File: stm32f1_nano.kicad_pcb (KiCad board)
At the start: 2 copper layers, 43.2 x 17.8 mm, 45 parts, among them J1 Analog, J2 Digital, J3 TYPE-C-31-M-12, J5 DEBUG, U1 STM32F103C8T6, U2 W25Q128JVSIQ, U4 XC6206P332MR, U5 AMS1117-5.0, Y1 X322516MLB4SI

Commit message: #2 green and red LED are too bright
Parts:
- R1, R2, R3: value 300 -> 330
- R11: value 75 -> 200
- R4: value 75 -> 150
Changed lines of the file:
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@@
     (descr "Resistor SMD 0402 (1005 Metric), square (rectangular) end terminal, IPC_7351 nominal, (Body size source: IPC-SM-782 page 72, https://www.pcb-3d.com/wordpress/wp-content/uploads/ipc-sm-782a_amendment_1_and_2.pdf), generated with kicad-footprint-generator")
     (tags "resistor")
-    (property "Description" "62.5mW Thick Film Resistors ±100ppm/℃ ±1% 300Ω 0402  Chip Resistor - Surface Mount ROHS")
-    (property "JLCPCB Part #" "C25102")
+    (property "Description" "62.5mW Thick Film Resistors ±100ppm/℃ ±1% 330Ω 0402  Chip Resistor - Surface Mount ROHS")
+    (property "JLCPCB Part #" "C25104")
     (property "Manufacturer" "UNI-ROYAL(Uniroyal Elec)")
-    (property "Manufacturer_Name" "UNI-ROYAL(Uniroyal Elec)")
-    (property "Manufacturer_Part_Number" "0402WGF3000TCE")
-    (property "Partnumber" "0402WGF3000TCE")
+    (property "Partnumber" "0402WGF3300TCE")
     (property "Sheetfile" "stm32f1_nano.kicad_sch")
     (property "Sheetname" "")
@@
         (effects (font (size 1 1) (thickness 0.15)))
     )
-    (fp_text value "300" (at 0 1.17) (layer "F.Fab")
+    (fp_text value "330" (at 0 1.17) (layer "F.Fab")
         (effects (font (size 1 1) (thickness 0.15)))
     )
@@
     (descr "Resistor SMD 0402 (1005 Metric), square (rectangular) end terminal, IPC_7351 nominal, (Body size source: IPC-SM-782 page 72, https://www.pcb-3d.com/wordpress/wp-content/uploads/ipc-sm-782a_amendment_1_and_2.pdf), generated with kicad-footprint-generator")
     (tags "resistor")
-    (property "Description" "62.5mW Thick Film Resistors ±100ppm/℃ ±1% 300Ω 0402  Chip Resistor - Surface Mount ROHS")
-    (property "JLCPCB Part #" "C25102")
+    (property "Description" "62.5mW Thick Film Resistors ±100ppm/℃ ±1% 330Ω 0402  Chip Resistor - Surface Mount ROHS")
+    (property "JLCPCB Part #" "C25104")
     (property "Manufacturer" "UNI-ROYAL(Uniroyal Elec)")
-    (property "Manufacturer_Name" "UNI-ROYAL(Uniroyal Elec)")
-    (property "Manufacturer_Part_Number" "0402WGF3000TCE")
-    (property "Partnumber" "0402WGF3000TCE")
+    (property "Partnumber" "0402WGF3300TCE")
     (property "Sheetfile" "stm32f1_nano.kicad_sch")
     (property "Sheetname" "")
@@
         (effects (font (size 1 1) (thickness 0.15)))
     )
-    (fp_text value "300" (at 0 1.17) (layer "F.Fab")
+    (fp_text value "330" (at 0 1.17) (layer "F.Fab")
         (effects (font (size 1 1) (thickness 0.15)))
     )
@@
     (descr "Resistor SMD 0402 (1005 Metric), square (rectangular) end terminal, IPC_7351 nominal, (Body size source: IPC-SM-782 page 72, https://www.pcb-3d.com/wordpress/wp-content/uploads/ipc-sm-782a_amendment_1_and_2.pdf), generated with kicad-footprint-generator")
     (tags "resistor")
-    (property "Description" "62.5mW Thick Film Resistors ±100ppm/℃ ±1% 75Ω 0402  Chip Resistor - Surface Mount ROHS")
-    (property "JLCPCB Part #" "C25133")
+    (property "Description" "62.5mW Thick Film Resistors ±100ppm/℃ ±1% 150Ω 0402  Chip Resistor - Surface Mount ROHS")
+    (property "JLCPCB Part #" "C25082")
     (property "Manufacturer" "UNI-ROYAL(Uniroyal Elec)")
-    (property "Manufacturer_Name" "UNI-ROYAL(Uniroyal Elec)")
-    (property "Manufacturer_Part_Number" "0402WGF750JTCE")
-    (property "Partnumber" "0402WGF750JTCE")
+    (property "Partnumber" "0402WGF1500TCE")
     (property "Sheetfile" "stm32f1_nano.kicad_sch")
     (property "Sheetname" "")
@@
         (effects (font (size 1 1) (thickness 0.15)))
     )
-    (fp_text value "75" (at 0 1.17) (layer "F.Fab")
+    (fp_text value "150" (at 0 1.17) (layer "F.Fab")
         (effects (font (size 1 1) (thickness 0.15)))
     )
@@
     (descr "Resistor SMD 0402 (1005 Metric), square (rectangular) end terminal, IPC_7351 nominal, (Body size source: IPC-SM-782 page 72, https://www.pcb-3d.com/wordpress/wp-content/uploads/ipc-sm-782a_amendment_1_and_2.pdf), generated with kicad-footprint-generator")
     (tags "resistor")
-    (property "Description" "62.5mW Thick Film Resistors ±100ppm/℃ ±1% 75Ω 0402  Chip Resistor - Surface Mount ROHS")
-    (property "JLCPCB Part #" "C25133")
+    (property "Description" "62.5mW Thick Film Resistors ±100ppm/℃ ±1% 200Ω 0402  Chip Resistor - Surface Mount ROHS")
+    (property "JLCPCB Part #" "C25087")
     (property "Manufacturer" "UNI-ROYAL(Uniroyal Elec)")
-    (property "Manufacturer_Name" "UNI-ROYAL(Uniroyal Elec)")
-    (property "Manufacturer_Part_Number" "0402WGF750JTCE")
-    (property "Partnumber" "0402WGF750JTCE")
+    (property "Partnumber" "0402WGF2000TCE")
     (property "Sheetfile" "stm32f1_nano.kicad_sch")
     (property "Sheetname" "")
@@
         (effects (font (size 1 1) (thickness 0.15)))
     )
-    (fp_text value "75" (at 0 1.17) (layer "F.Fab")
+    (fp_text value "200" (at 0 1.17) (layer "F.Fab")
         (effects (font (size 1 1) (thickness 0.15)))
     )
@@
     (descr "Resistor SMD 0402 (1005 Metric), square (rectangular) end terminal, IPC_7351 nominal, (Body size source: IPC-SM-782 page 72, https://www.pcb-3d.com/wordpress/wp-content/uploads/ipc-sm-782a_amendment_1_and_2.pdf), generated with kicad-footprint-generator")
     (tags "resistor")
-    (property "Description" "62.5mW Thick Film Resistors ±100ppm/℃ ±1% 300Ω 0402  Chip Resistor - Surface Mount ROHS")
-    (property "JLCPCB Part #" "C25102")
+    (property "Description" "62.5mW Thick Film Resistors ±100ppm/℃ ±1% 330Ω 0402  Chip Resistor - Surface Mount ROHS")
+    (property "JLCPCB Part #" "C25104")
     (property "Manufacturer" "UNI-ROYAL(Uniroyal Elec)")
-    (property "Manufacturer_Name" "UNI-ROYAL(Uniroyal Elec)")
-    (property "Manufacturer_Part_Number" "0402WGF3000TCE")
-    (property "Partnumber" "0402WGF3000TCE")
+    (property "Partnumber" "0402WGF3300TCE")
     (property "Sheetfile" "stm32f1_nano.kicad_sch")
     (property "Sheetname" "")
@@
         (effects (font (size 1 1) (thickness 0.15)))
     )
-    (fp_text value "300" (at 0 1.17) (layer "F.Fab")
-        (effects (font (size 1 1) (thickness 0.15)))
-    )
+    (fp_text value "330" (at 0 1.17) (layer "F.Fab")
+        (effects (font (size 1 1) (thickness 0.15)))
+    )

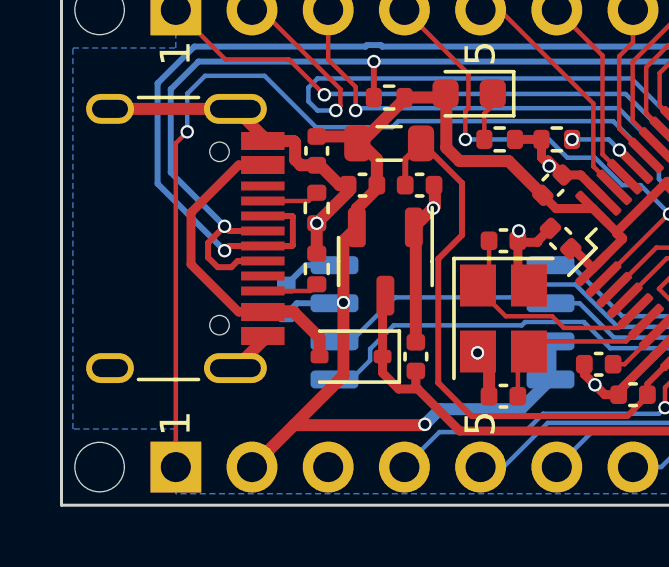
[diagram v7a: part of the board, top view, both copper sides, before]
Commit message: #3 Make C12 bigger or move to Front
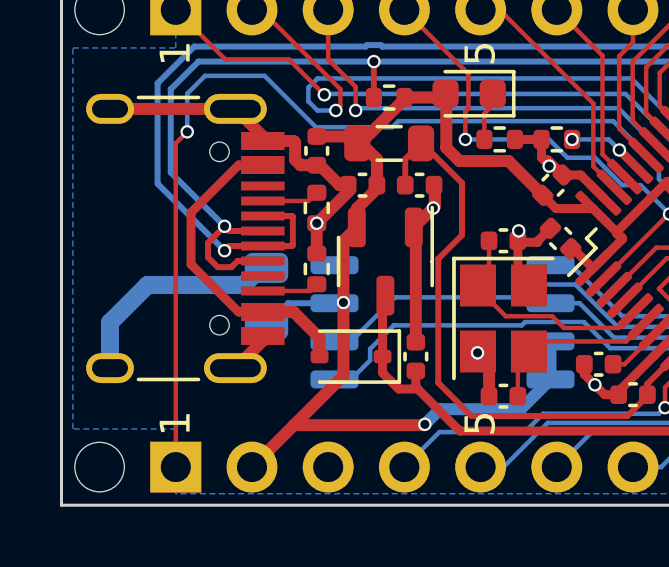
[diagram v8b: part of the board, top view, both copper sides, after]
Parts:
- C12: value 100n 16V -> 100n 100V; footprint Capacitor_SMD:C_0402_1005Metric -> Capacitor_SMD:C_0805_2012Metric
- moved C12 0.67 mm to (106.8, 93.0), turned to -90 degrees
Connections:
- C12 pad 1: +3.3V -> GND
- C12 pad 2: GND -> +3.3V
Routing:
- net GND: track 44.2 -> 49.8 mm
- net +3.3V: track 81.6 -> 82.5 mm
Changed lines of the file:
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@@
     )
   )
-  (footprint "Capacitor_SMD:C_0402_1005Metric" (layer "B.Cu")
-    (at 107.493 93.142 90)
-    (descr "Capacitor SMD 0402 (1005 Metric), square (rectangular) end terminal, IPC_7351 nominal, (Body size source: IPC-SM-782 page 76, https://www.pcb-3d.com/wordpress/wp-content/uploads/ipc-sm-782a_amendment_1_and_2.pdf), generated with kicad-footprint-generator")
+  (footprint "Capacitor_SMD:C_0805_2012Metric" (layer "B.Cu")
+    (at 106.8326 93.0404 -90)
+    (descr "Capacitor SMD 0805 (2012 Metric), square (rectangular) end terminal, IPC_7351 nominal, (Body size source: IPC-SM-782 page 76, https://www.pcb-3d.com/wordpress/wp-content/uploads/ipc-sm-782a_amendment_1_and_2.pdf, https://docs.google.com/spreadsheets/d/1BsfQQcO9C6DZCsRaXUlFlo91Tg2WpOkGARC1WS5S8t0/edit?usp=sharing), generated with kicad-footprint-generator")
     (tags "capacitor")
-    (property "Description" "16V 100nF X7R ±10% 0402  Multilayer Ceramic Capacitors MLCC - SMD/SMT ROHS")
-    (property "JLCPCB Part #" "C1525")
+    (property "Description" "100V 100nF X7R ±10% 0805  Multilayer Ceramic Capacitors MLCC - SMD/SMT ROHS")
+    (property "JLCPCB Part #" "C28233")
     (property "Manufacturer" "Samsung Electro-Mechanics")
-    (property "Partnumber" "CL05B104KO5NNNC")
+    (property "Manufacturer_Name" "Samsung Electro-Mechanics")
+    (property "Manufacturer_Part_Number" "CL21B104KCFNNNE")
+    (property "Partnumber" "CL21B104KCFNNNE")
     (property "Sheetfile" "stm32f1_nano.kicad_sch")
     (property "Sheetname" "")
@@
     (property "ki_keywords" "capacitor cap")
     (attr smd exclude_from_bom)
-    (fp_text reference "C12" (at 0 -1.778 90) (layer "B.SilkS")
+    (fp_text reference "C12" (at -2.0574 -0.0254 -180) (layer "B.SilkS")
         (effects (font (size 0.4 0.4) (thickness 0.05)) (justify mirror))
     )
-    (fp_text value "100n 16V" (at 0 -1.16 90) (layer "B.SilkS")
+    (fp_text value "100n 100V" (at -2.7178 0 -180) (layer "B.SilkS")
         (effects (font (size 0.4 0.3) (thickness 0.05)) (justify mirror))
     )
     (fp_text user "${REFERENCE}" (at 0 0 90) (layer "B.Fab")
-        (effects (font (size 0.25 0.25) (thickness 0.04)) (justify mirror))
-    )
-    (fp_line (start -0.107836 -0.36) (end 0.107836 -0.36)
+        (effects (font (size 0.5 0.5) (thickness 0.08)) (justify mirror))
+    )
+    (fp_line (start -0.261252 -0.735) (end 0.261252 -0.735)
       (stroke (width 0.12) (type solid)) (layer "B.SilkS"))
-    (fp_line (start -0.107836 0.36) (end 0.107836 0.36)
+    (fp_line (start -0.261252 0.735) (end 0.261252 0.735)
       (stroke (width 0.12) (type solid)) (layer "B.SilkS"))
-    (fp_line (start -0.91 -0.46) (end -0.91 0.46)
+    (fp_line (start -1.7 -0.98) (end -1.7 0.98)
       (stroke (width 0.05) (type solid)) (layer "B.CrtYd"))
-    (fp_line (start -0.91 0.46) (end 0.91 0.46)
+    (fp_line (start -1.7 0.98) (end 1.7 0.98)
       (stroke (width 0.05) (type solid)) (layer "B.CrtYd"))
-    (fp_line (start 0.91 -0.46) (end -0.91 -0.46)
+    (fp_line (start 1.7 -0.98) (end -1.7 -0.98)
       (stroke (width 0.05) (type solid)) (layer "B.CrtYd"))
-    (fp_line (start 0.91 0.46) (end 0.91 -0.46)
+    (fp_line (start 1.7 0.98) (end 1.7 -0.98)
       (stroke (width 0.05) (type solid)) (layer "B.CrtYd"))
-    (fp_line (start -0.5 -0.25) (end -0.5 0.25)
+    (fp_line (start -1 -0.625) (end -1 0.625)
       (stroke (width 0.1) (type solid)) (layer "B.Fab"))
-    (fp_line (start -0.5 0.25) (end 0.5 0.25)
+    (fp_line (start -1 0.625) (end 1 0.625)
       (stroke (width 0.1) (type solid)) (layer "B.Fab"))
-    (fp_line (start 0.5 -0.25) (end -0.5 -0.25)
+    (fp_line (start 1 -0.625) (end -1 -0.625)
       (stroke (width 0.1) (type solid)) (layer "B.Fab"))
-    (fp_line (start 0.5 0.25) (end 0.5 -0.25)
+    (fp_line (start 1 0.625) (end 1 -0.625)
       (stroke (width 0.1) (type solid)) (layer "B.Fab"))
-    (pad "1" smd roundrect (at -0.48 0 90) (size 0.56 0.62) (layers "B.Cu" "B.Paste" "B.Mask") (roundrect_rratio 0.25)
+    (pad "1" smd roundrect (at -0.95 0 270) (size 1 1.45) (layers "B.Cu" "B.Paste" "B.Mask") (roundrect_rratio 0.25)
+      (net 1 "GND") (pintype "passive"))
+    (pad "2" smd roundrect (at 0.95 0 270) (size 1 1.45) (layers "B.Cu" "B.Paste" "B.Mask") (roundrect_rratio 0.25)
       (net 3 "+3.3V") (pintype "passive"))
-    (pad "2" smd roundrect (at 0.48 0 90) (size 0.56 0.62) (layers "B.Cu" "B.Paste" "B.Mask") (roundrect_rratio 0.25)
-      (net 1 "GND") (pintype "passive"))
-    (model "${KICAD6_3DMODEL_DIR}/Capacitor_SMD.3dshapes/C_0402_1005Metric.wrl"
+    (model "${KICAD6_3DMODEL_DIR}/Capacitor_SMD.3dshapes/C_0805_2012Metric.wrl"
       (offset (xyz 0 0 0))
       (scale (xyz 1 1 1))
@@
   (via micro (at 115.24 90.856) (size 0.45) (drill 0.3) (layers "F.Cu" "B.Cu") (net 1))
   (via micro (at 135.066 95.53) (size 0.45) (drill 0.3) (layers "F.Cu" "B.Cu") (net 1))
-  (segment (start 107.493 92.662) (end 108.156 91.999) (width 0.2) (layer "B.Cu") (net 1))
-  (segment (start 108.156 91.999) (end 109.1 91.999) (width 0.2) (layer "B.Cu") (net 1))
+  (segment (start 101.617 93.9126) (end 102.8702 92.6594) (width 0.6) (layer "B.Cu") (net 1))
+  (segment (start 102.8702 92.6594) (end 106.0706 92.6594) (width 0.6) (layer "B.Cu") (net 1))
+  (segment (start 106.6396 92.0904) (end 106.8326 92.0904) (width 0.6) (layer "B.Cu") (net 1))
+  (segment (start 101.617 95.43) (end 101.617 93.9126) (width 0.6) (layer "B.Cu") (net 1))
+  (segment (start 106.0706 92.6594) (end 106.6396 92.0904) (width 0.6) (layer "B.Cu") (net 1))
   (segment (start 131.564324 97.555) (end 131.164524 97.1552) (width 0.15) (layer "F.Cu") (net 2))
   (segment (start 120.407382 93.280182) (end 120.407382 93.662172) (width 0.15) (layer "F.Cu") (net 2))
@@
   (via micro (at 112.11269 97.305554) (size 0.45) (drill 0.3) (layers "F.Cu" "B.Cu") (net 3))
   (via micro (at 109.398 93.2436) (size 0.45) (drill 0.3) (layers "F.Cu" "B.Cu") (net 3))
+  (segment (start 106.8326 93.9904) (end 107.554 93.269) (width 0.2) (layer "B.Cu") (net 3))
   (segment (start 112.11269 97.305554) (end 112.618644 96.7996) (width 0.4) (layer "B.Cu") (net 3))
   (segment (start 112.618644 96.7996) (end 115.3094 96.7996) (width 0.4) (layer "B.Cu") (net 3))
+  (segment (start 107.554 93.269) (end 109.1 93.269) (width 0.2) (layer "B.Cu") (net 3))
   (segment (start 116.3 95.809) (end 116.3 94.539) (width 0.4) (layer "B.Cu") (net 3))
-  (segment (start 107.846 93.269) (end 109.1 93.269) (width 0.2) (layer "B.Cu") (net 3))
   (segment (start 115.3094 96.7996) (end 116.3 95.809) (width 0.4) (layer "B.Cu") (net 3))
-  (segment (start 107.493 93.622) (end 107.846 93.269) (width 0.2) (layer "B.Cu") (net 3))
   (segment (start 112.558 91.790239) (end 112.558 95.921) (width 0.2) (layer "F.Cu") (net 4))
   (segment (start 112.558 95.921) (end 113.6648 97.0278) (width 0.2) (layer "F.Cu") (net 4))
